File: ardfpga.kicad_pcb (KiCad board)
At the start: 2 copper layers, 69 x 53.8 mm, 69 parts, among them J1 AD, J2 PWR, J3 ICSP, J4 USB, J5 POWER, Q1 NMOS, Q2 NMOS, U1 iCE40LP384, U2 AT25xxx, U3 ATMega328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

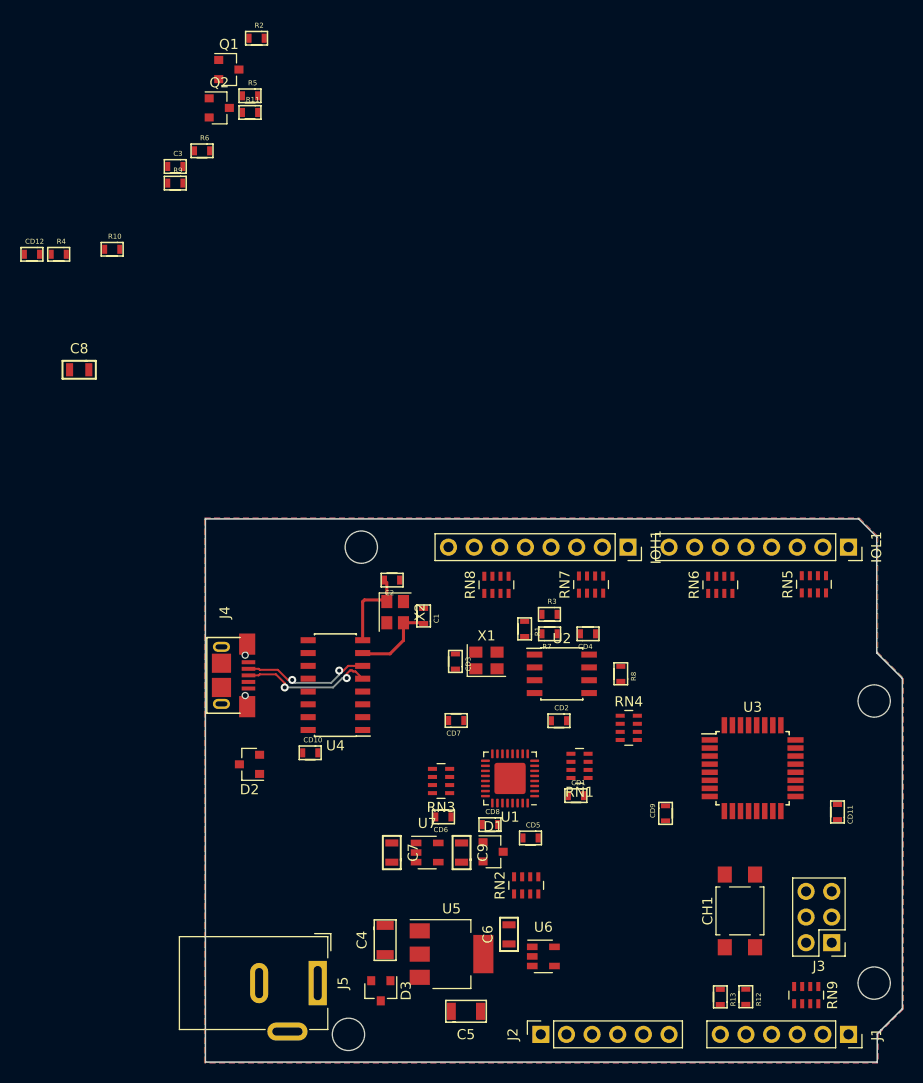
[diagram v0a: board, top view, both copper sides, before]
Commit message: Added 3d image of the board for github README file.
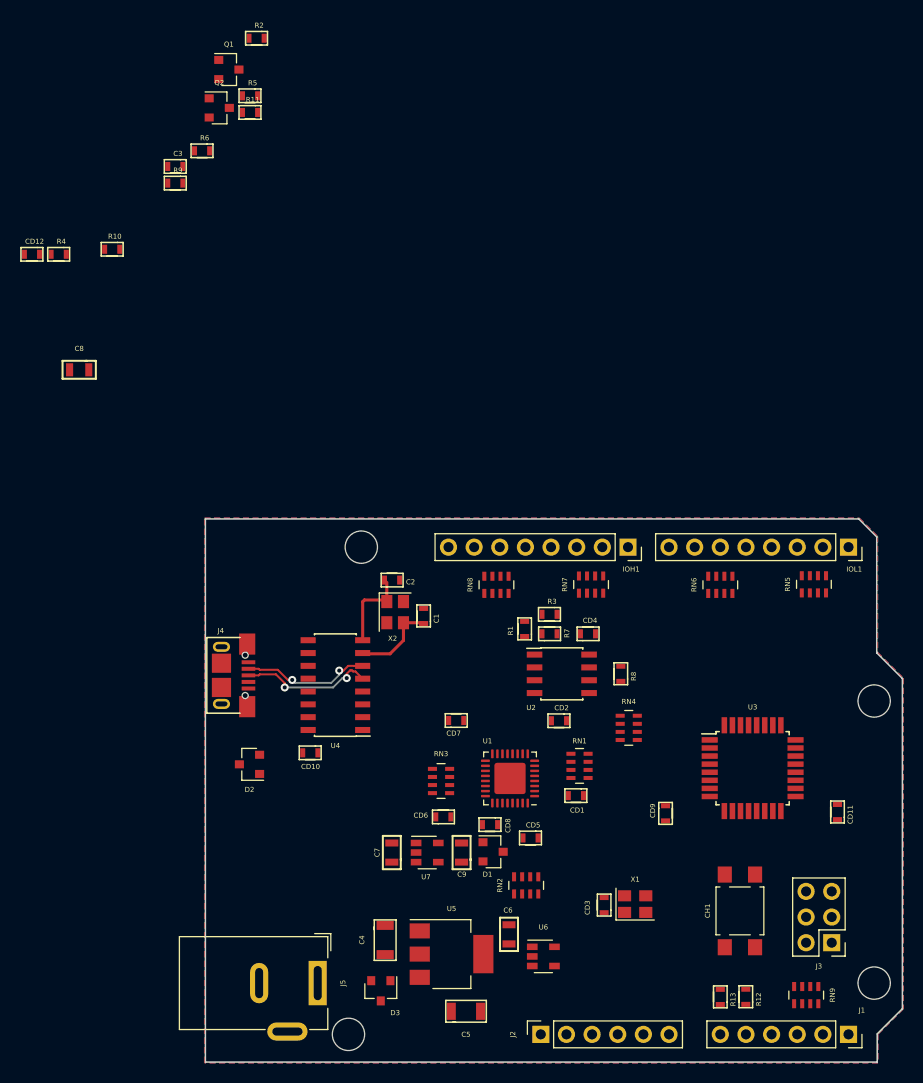
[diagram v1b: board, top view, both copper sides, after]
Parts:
- moved CD3 28.3 mm to (107.8, 119.9)
- moved X1 28.3 mm to (110.9, 119.8)

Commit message: Board routed, circuit changed to ease PCB routing. Minor adjustments. Ready to re-check PCB.
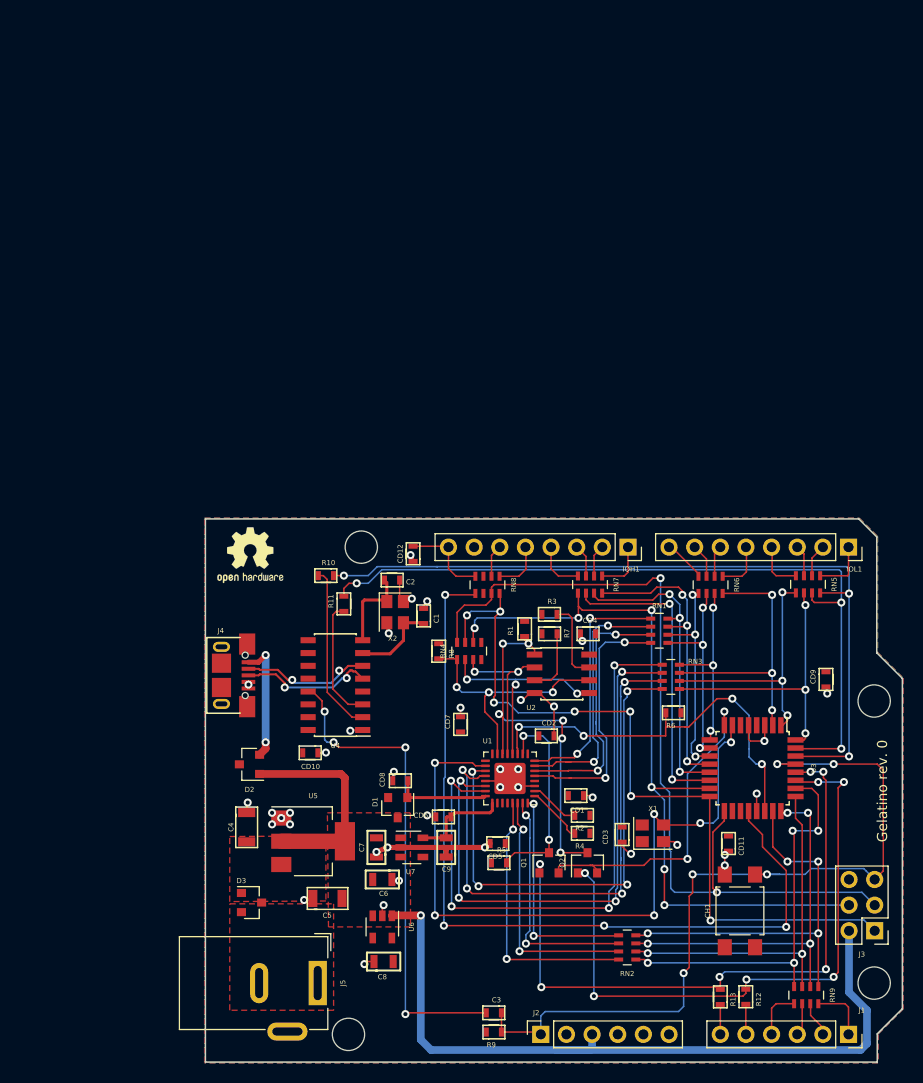
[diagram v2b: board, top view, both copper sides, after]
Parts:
- added REF**: OSHW-Logo2_7.3x6mm_SilkScreen, Symbol:OSHW-Logo2_7.3x6mm_SilkScreen, F.Cu at (72.8, 85.2)
- moved R9 89.8 mm to (96.9, 132.5), turned to 180 degrees
- moved C3 89.6 mm to (96.9, 130.6)
- moved Q1 84.7 mm to (102.4, 115.7), turned to 90 degrees
- moved R2 83.5 mm to (105.7, 111.0), turned to 180 degrees
- moved Q2 83.2 mm to (106.2, 115.7), turned to 90 degrees
- moved R5 79.9 mm to (97.4, 115.7)
- moved R4 77.3 mm to (105.7, 112.8), turned to 180 degrees
- moved R6 72.6 mm to (114.7, 100.8), turned to 180 degrees
- moved C8 65.9 mm to (86.0, 125.5), turned to 180 degrees
- moved R11 49.6 mm to (82.0, 90.0), turned to 90 degrees
- moved CD12 48.0 mm to (88.9, 85.1), turned to 270 degrees
- moved R10 38.6 mm to (80.3, 87.2)
- moved RN3 25.0 mm to (114.4, 97.3), turned to 0 degrees
- moved CD9 20.7 mm to (129.8, 97.5)
- moved R8 18.2 mm to (91.4, 94.7)
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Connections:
- IOH1 pad 7: Net-(IOH1-Pad7) -> GND
- J2 pad 6: Net-(J2-Pad6) -> (no net)
- R2 pad 1: IO8 -> (no net)
- R4 pad 1: IO9 -> (no net)
- RN1 pad 1: AD0 -> IO6
- RN1 pad 2: AD1 -> IO7
- RN1 pad 3: AD2 -> IO8
- RN1 pad 4: AD3 -> IO9
- RN2 pad 1: IO3 -> AD3
- RN2 pad 2: IO2 -> AD2
- RN2 pad 3: IO1 -> AD1
- RN2 pad 4: IO0 -> AD0
- RN3 pad 5: IO7 -> IO2
- RN3 pad 6: IO6 -> IO3
- RN3 pad 7: IO5 -> IO4
- RN3 pad 8: IO4 -> IO5
- RN4 pad 4: Net-(RN4-Pad4) -> (no net)
- RN4 pad 5: Net-(RN4-Pad5) -> (no net)
- RN5 pad 1: IO0 -> Net-(IOL1-Pad1)
- RN5 pad 2: IO1 -> Net-(IOL1-Pad2)
- RN5 pad 3: IO2 -> Net-(IOL1-Pad3)
- RN5 pad 4: IO3 -> Net-(IOL1-Pad4)
- RN5 pad 5: Net-(IOL1-Pad4) -> IO3
- RN5 pad 6: Net-(IOL1-Pad3) -> IO2
- RN5 pad 7: Net-(IOL1-Pad2) -> IO1
- RN5 pad 8: Net-(IOL1-Pad1) -> IO0
- RN6 pad 1: IO4 -> Net-(IOL1-Pad5)
- RN6 pad 2: IO5 -> Net-(IOL1-Pad6)
- RN6 pad 3: IO6 -> Net-(IOL1-Pad7)
- RN6 pad 4: IO7 -> Net-(IOL1-Pad8)
- RN6 pad 5: Net-(IOL1-Pad8) -> IO7
- RN6 pad 6: Net-(IOL1-Pad7) -> IO6
- RN6 pad 7: Net-(IOL1-Pad6) -> IO5
- RN6 pad 8: Net-(IOL1-Pad5) -> IO4
- RN7 pad 1: IO8 -> Net-(IOH1-Pad1)
- RN7 pad 2: IO9 -> Net-(IOH1-Pad2)
- RN7 pad 3: MSS -> Net-(IOH1-Pad3)
- RN7 pad 4: MSDO -> Net-(IOH1-Pad4)
- RN7 pad 5: Net-(IOH1-Pad4) -> MSDO
- RN7 pad 6: Net-(IOH1-Pad3) -> MSS
- RN7 pad 7: Net-(IOH1-Pad2) -> IO9
- RN7 pad 8: Net-(IOH1-Pad1) -> IO8
- RN8 pad 1: MSDI -> Net-(IOH1-Pad5)
- RN8 pad 2: MSCK -> Net-(IOH1-Pad6)
- RN8 pad 3: GND -> (no net)
- RN8 pad 4: AREF -> Net-(CD12-Pad1)
- RN8 pad 5: Net-(CD12-Pad1) -> AREF
- RN8 pad 6: Net-(IOH1-Pad7) -> (no net)
- RN8 pad 7: Net-(IOH1-Pad6) -> MSCK
- RN8 pad 8: Net-(IOH1-Pad5) -> MSDI
- U1 pad 26: Net-(U1-Pad26) -> (no net)
- U1 pad 27: Net-(U1-Pad27) -> (no net)
- U3 pad 19: Net-(U3-Pad19) -> (no net)
- U4 pad 10: Net-(U4-Pad10) -> (no net)
- U4 pad 11: Net-(U4-Pad11) -> (no net)
- U4 pad 12: Net-(U4-Pad12) -> (no net)
- U4 pad 14: Net-(U4-Pad14) -> (no net)
- U4 pad 15: Net-(U4-Pad15) -> (no net)
- U4 pad 9: Net-(U4-Pad9) -> (no net)
- X2 pad 2: GND -> Net-(C1-Pad2)
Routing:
- net +5V: track 0.00 -> 98.1 mm, vias 0 -> 1
- net MSCK: track 0.00 -> 86.0 mm, vias 0 -> 2
- net AREF: track 0.00 -> 82.8 mm, vias 0 -> 4
- net MRST: track 0.00 -> 80.6 mm, vias 0 -> 5
- net IO0: track 0.00 -> 78.4 mm, vias 0 -> 3
- net IO1: track 0.00 -> 76.7 mm, vias 0 -> 3
- net MSDI: track 0.00 -> 76.6 mm, vias 0 -> 7
- net MSDO: track 0.00 -> 76.3 mm, vias 0 -> 6
- net CLK16: track 0.00 -> 69.3 mm, vias 0 -> 6
- net AD5: track 0.00 -> 65.5 mm, vias 0 -> 6
- net AD4: track 0.00 -> 63.2 mm, vias 0 -> 6
- net Net-(RN3-Pad1): track 0.00 -> 61.0 mm, vias 0 -> 4
- net Net-(RN3-Pad2): track 0.00 -> 57.0 mm, vias 0 -> 4
- net Net-(RN3-Pad3): track 0.00 -> 55.5 mm, vias 0 -> 4
- net GND: track 0.00 -> 55.1 mm, vias 0 -> 38
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- added copper zone on F.Cu, net +5V
- added copper zone on F.Cu, net Net-(D3-Pad2)
- added copper zone on F.Cu, net V+
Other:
- board text added: "Gelatino rev. 0"

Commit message: Board revision, leds added. Better routing.
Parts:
- added D4: LED_Small_ALT, mylib:0603_LED, F.Cu at (133.2, 107.8)
- added D5: LED_Small_ALT, mylib:0603_LED, F.Cu at (133.2, 110.7)
- added G***: LOGO, logo:wiselogo1, F.Cu at (157.9, 101.7)
- added G***: LOGO, logo:wiselogo1, B.Cu at (73.4, 85.6)
- added R14: 220, mylib:0603_RES, F.Cu at (133.2, 104.9)
- added R15: 220, mylib:0603_RES, F.Cu at (133.2, 113.7)
- moved CD6 4.61 mm to (96.5, 111.8), turned to 0 degrees
- moved CD9 3.08 mm to (127.9, 99.9), turned to 180 degrees
- moved CD2 1.21 mm to (103.3, 103.2)
- turned R6 to 0 degrees
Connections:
- R2 pad 1: (no net) -> IO0
- R4 pad 1: (no net) -> IO1
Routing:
- net IO1: track 76.7 -> 107.7 mm, vias 3 -> 4
- net IO0: track 78.4 -> 109.3 mm, vias 3 -> 6
- net AD4: track 63.2 -> 69.2 mm
- net MSCK: track 86.0 -> 91.9 mm
- net IO4: track 27.1 -> 22.5 mm, vias 3 -> 4
- net AD3: track 39.9 -> 44.1 mm, vias 4 -> 5
- net AD5: track 65.5 -> 69.5 mm
- net AD0: track 39.2 -> 36.1 mm, vias 4 -> 3
- net AD1: track 37.3 -> 35.6 mm, vias 4 -> 3
- net Net-(D5-Pad2): track 0.00 -> 1.42 mm
- net Net-(D4-Pad2): track 0.00 -> 1.42 mm
- net Net-(RN1-Pad6): track 25.8 -> 24.4 mm
- net Net-(RN3-Pad1): track 61.0 -> 59.9 mm
- net FSS: track 38.8 -> 37.8 mm, vias 6 -> 4
- net GND: track 55.1 -> 56.1 mm, vias 38 -> 40
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
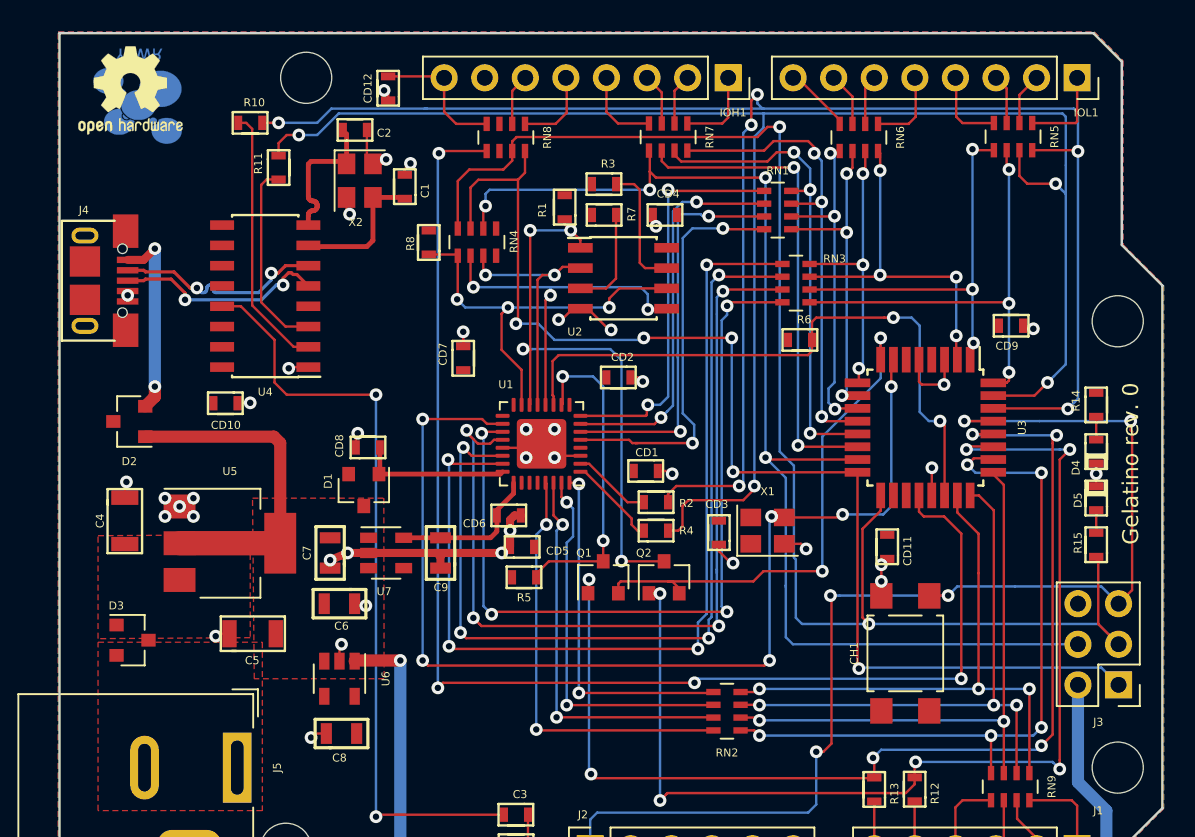
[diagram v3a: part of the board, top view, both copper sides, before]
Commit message: Bugs in the board corrected. Better routing. First BOM version.
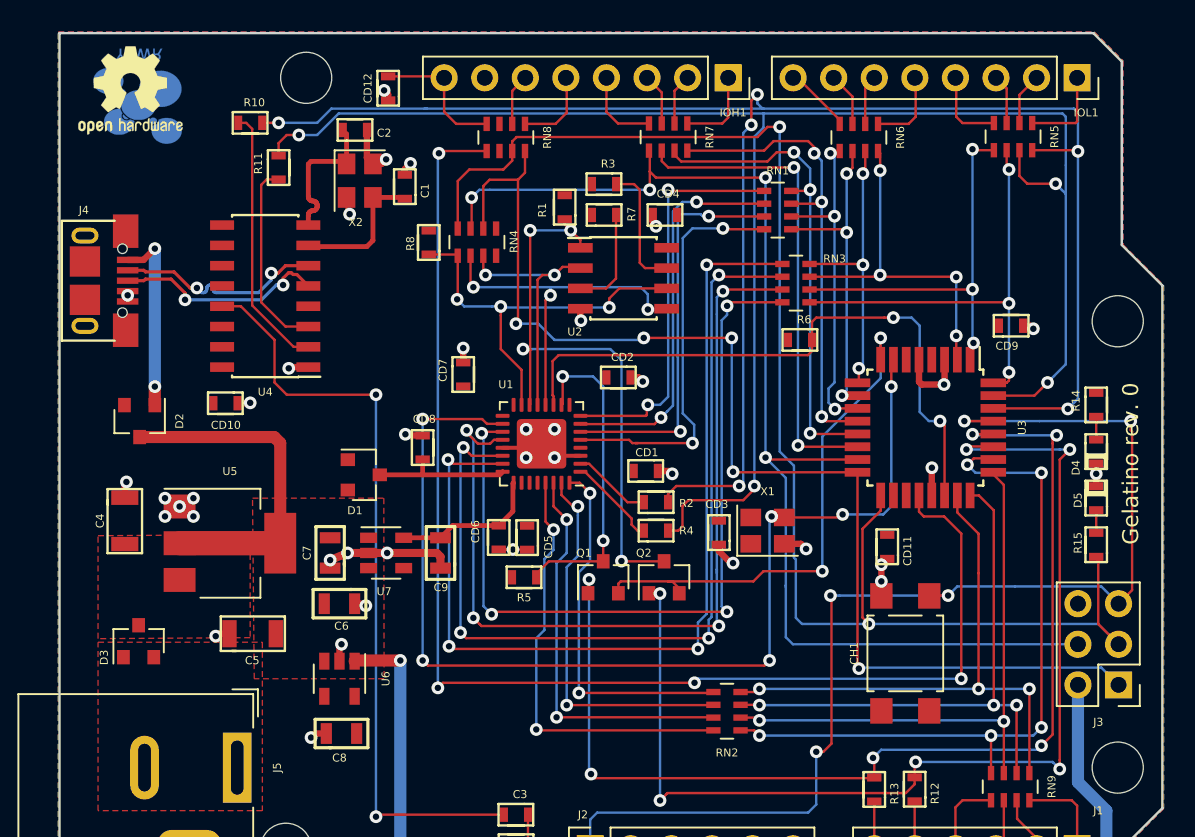
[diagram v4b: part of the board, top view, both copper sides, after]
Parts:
- moved CD8 3.43 mm to (91.1, 107.6), turned to 90 degrees
- moved CD6 1.52 mm to (95.8, 113.2), turned to 270 degrees
- moved CD7 1.02 mm to (93.6, 103.0)
- moved D1 0.95 mm to (87.4, 109.3), turned to 0 degrees
- moved CD5 0.65 mm to (97.6, 113.2), turned to 270 degrees
- moved D2 0.65 mm to (73.3, 105.9), turned to 270 degrees
- moved D3 0.39 mm to (73.3, 119.7), turned to 90 degrees
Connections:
- D1 pad 1: Net-(CD8-Pad1) -> +3.3V
- D1 pad 2: +3.3V -> (no net)
- D1 pad 3: (no net) -> Net-(CD8-Pad1)
- D2 pad 1: +5V -> Net-(D2-Pad2)
- D2 pad 2: Net-(D2-Pad2) -> (no net)
- D2 pad 3: (no net) -> +5V
- D3 pad 1: V+ -> Net-(D3-Pad2)
- D3 pad 2: Net-(D3-Pad2) -> (no net)
- D3 pad 3: (no net) -> V+
- RN4 pad 6: MSDO -> MSDI
- RN4 pad 7: MSDI -> MSDO
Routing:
- net GND: track 56.1 -> 47.8 mm, vias 40 -> 39
- net MSDI: track 76.0 -> 75.3 mm
- net MSDO: track 76.2 -> 76.9 mm
- net Net-(RN2-Pad5): track 22.1 -> 22.8 mm
